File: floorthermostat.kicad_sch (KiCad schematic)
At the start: 29 parts, among them J1 Temp sensor socket 3 pin, J2 spi7segdisp, J3 Conn_01x06_Socket, J5 Programmin connector, Q1 BC549, SW1 Reset pushbutton, SW2 Enable pushbutton, U1 ESP32-WROOM-32, U2 GOLD 240V 3A SSR, U3 BD33FC0FP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

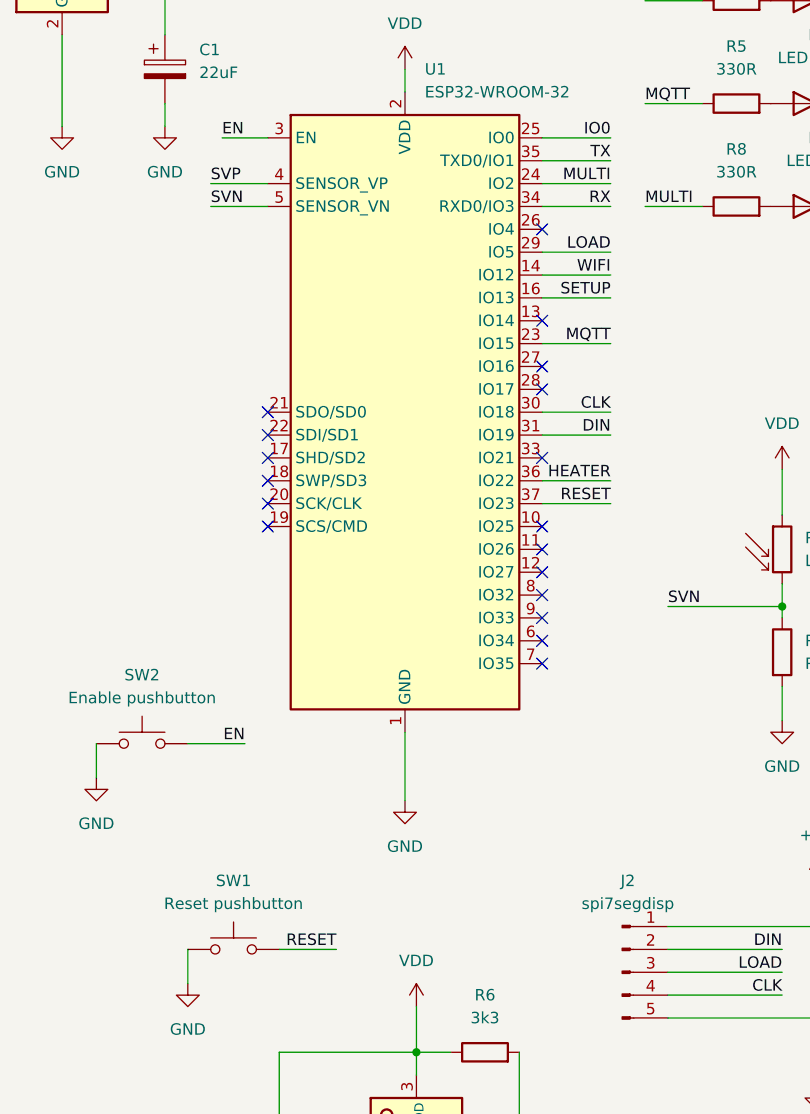
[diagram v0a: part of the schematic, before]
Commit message: Changed pcb to dual-sided.
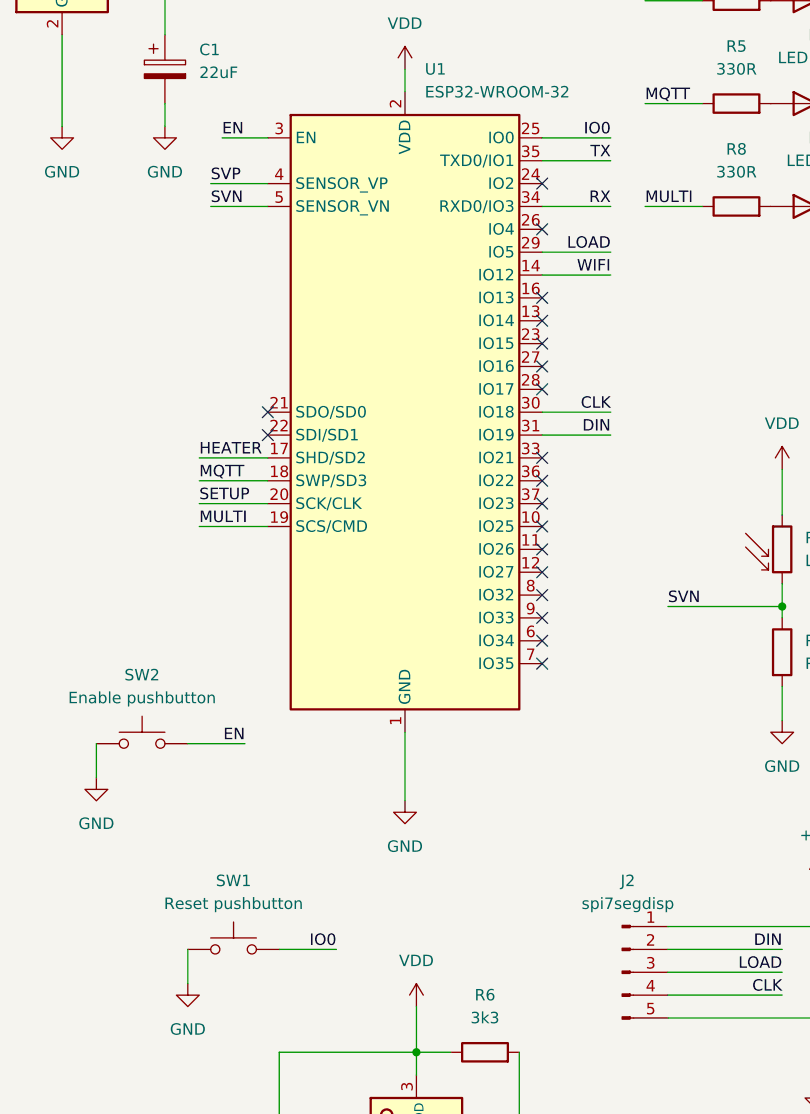
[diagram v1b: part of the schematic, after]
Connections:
- net HEATER: now also U1.17 (SHD/SD2); no longer U1.36 (IO22)
- net IO0: now also SW1.2
- net MQTT: now also U1.18 (SWP/SD3); no longer U1.23 (IO15)
- net MULTI: now also U1.19 (SCS/CMD); no longer U1.24 (IO2)
- net SETUP: now also U1.20 (SCK/CLK); no longer U1.16 (IO13)
- net RESET: no longer names the net of U1.37 (IO23)
- net RESET: no longer SW1.2
- no-connect marks 18 -> 19
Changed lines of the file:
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@@
+	)
+	(no_connect
+		(at 128.27 54.61)
 	)
 	(no_connect
@@
 	)
 	(no_connect
-		(at 97.79 87.63)
-	)
-	(no_connect
 		(at 128.27 69.85)
 	)
@@
 	)
 	(no_connect
+		(at 128.27 72.39)
+	)
+	(no_connect
 		(at 97.79 82.55)
 	)
@@
 	)
 	(no_connect
+		(at 128.27 90.17)
+	)
+	(no_connect
+		(at 128.27 67.31)
+	)
+	(no_connect
+		(at 128.27 105.41)
+	)
+	(no_connect
+		(at 128.27 74.93)
+	)
+	(no_connect
+		(at 128.27 85.09)
+	)
+	(no_connect
+		(at 128.27 59.69)
+	)
+	(no_connect
 		(at 128.27 77.47)
 	)
 	(no_connect
-		(at 97.79 90.17)
-	)
-	(no_connect
-		(at 128.27 105.41)
-	)
-	(no_connect
-		(at 128.27 74.93)
-	)
-	(no_connect
-		(at 128.27 85.09)
-	)
-	(no_connect
-		(at 128.27 59.69)
-	)
-	(no_connect
 		(at 128.27 92.71)
 	)
@@
 	)
 	(no_connect
-		(at 97.79 92.71)
-	)
-	(no_connect
 		(at 128.27 107.95)
 	)
@@
 	)
 	(no_connect
-		(at 97.79 85.09)
+		(at 128.27 87.63)
 	)
 	(wire
@@
 	(wire
 		(pts
-			(xy 128.27 90.17) (xy 135.89 90.17)
-		)
-		(stroke
-			(width 0)
-			(type default)
-		)
-	)
-	(wire
-		(pts
 			(xy 63.5 30.48) (xy 67.31 30.48)
 		)
@@
 	(wire
 		(pts
+			(xy 90.17 90.17) (xy 97.79 90.17)
+		)
+		(stroke
+			(width 0)
+			(type default)
+		)
+	)
+	(wire
+		(pts
 			(xy 125.73 175.26) (xy 125.73 161.29)
 		)
@@
 	(wire
 		(pts
-			(xy 128.27 87.63) (xy 135.89 87.63)
-		)
-		(stroke
-			(width 0)
-			(type default)
-		)
-	)
-	(wire
-		(pts
 			(xy 232.41 67.31) (xy 224.79 67.31)
 		)
@@
 	(wire
 		(pts
+			(xy 90.17 85.09) (xy 97.79 85.09)
+		)
+		(stroke
+			(width 0)
+			(type default)
+		)
+	)
+	(wire
+		(pts
 			(xy 92.71 177.8) (xy 114.3 177.8)
 		)
@@
 	(wire
 		(pts
-			(xy 128.27 54.61) (xy 135.89 54.61)
-		)
-		(stroke
-			(width 0)
-			(type default)
-		)
-	)
-	(wire
-		(pts
 			(xy 224.79 96.52) (xy 232.41 96.52)
 		)
@@
 	(wire
 		(pts
-			(xy 128.27 72.39) (xy 135.89 72.39)
-		)
-		(stroke
-			(width 0)
-			(type default)
-		)
-	)
-	(wire
-		(pts
-			(xy 128.27 67.31) (xy 135.89 67.31)
-		)
-		(stroke
-			(width 0)
-			(type default)
-		)
-	)
-	(wire
-		(pts
 			(xy 74.93 38.1) (xy 74.93 48.26)
 		)
@@
 	(wire
 		(pts
+			(xy 90.17 92.71) (xy 97.79 92.71)
+		)
+		(stroke
+			(width 0)
+			(type default)
+		)
+	)
+	(wire
+		(pts
 			(xy 207.01 46.99) (xy 207.01 50.8)
 		)
@@
 		(pts
 			(xy 229.87 60.96) (xy 232.41 60.96)
+		)
+		(stroke
+			(width 0)
+			(type default)
+		)
+	)
+	(wire
+		(pts
+			(xy 90.17 87.63) (xy 97.79 87.63)
 		)
 		(stroke
@@
 		)
 	)
-	(label "RESET"
-		(at 135.89 90.17 180)
-		(fields_autoplaced yes)
-		(effects
-			(font
-				(size 1.27 1.27)
-			)
-			(justify right bottom)
-		)
-	)
 	(label "LOAD"
 		(at 154.94 142.24 180)
@@
 	)
 	(label "SETUP"
-		(at 135.89 67.31 180)
-		(fields_autoplaced yes)
-		(effects
-			(font
-				(size 1.27 1.27)
-			)
-			(justify right bottom)
+		(at 90.17 90.17 0)
+		(fields_autoplaced yes)
+		(effects
+			(font
+				(size 1.27 1.27)
+			)
+			(justify left bottom)
+		)
+	)
+	(label "MQTT"
+		(at 90.17 87.63 0)
+		(fields_autoplaced yes)
+		(effects
+			(font
+				(size 1.27 1.27)
+			)
+			(justify left bottom)
+		)
+	)
+	(label "HEATER"
+		(at 90.17 85.09 0)
+		(fields_autoplaced yes)
+		(effects
+			(font
+				(size 1.27 1.27)
+			)
+			(justify left bottom)
 		)
 	)
@@
 		)
 	)
+	(label "MULTI"
+		(at 90.17 92.71 0)
+		(fields_autoplaced yes)
+		(effects
+			(font
+				(size 1.27 1.27)
+			)
+			(justify left bottom)
+		)
+	)
 	(label "WIFI"
 		(at 135.89 64.77 180)
@@
 		)
 	)
-	(label "MULTI"
-		(at 135.89 54.61 180)
-		(fields_autoplaced yes)
-		(effects
-			(font
-				(size 1.27 1.27)
-			)
-			(justify right bottom)
-		)
-	)
 	(label "IO0"
 		(at 213.36 41.91 180)
@@
 		)
 	)
-	(label "MQTT"
-		(at 135.89 72.39 180)
-		(fields_autoplaced yes)
-		(effects
-			(font
-				(size 1.27 1.27)
-			)
-			(justify right bottom)
-		)
-	)
 	(label "IO0"
 		(at 135.89 49.53 180)
@@
 		)
 	)
-	(label "HEATER"
-		(at 135.89 87.63 180)
-		(fields_autoplaced yes)
-		(effects
-			(font
-				(size 1.27 1.27)
-			)
-			(justify right bottom)
-		)
-	)
 	(label "ACN"
 		(at 217.17 119.38 0)
@@
 		)
 	)
-	(label "RESET"
+	(label "IO0"
 		(at 105.41 139.7 180)
 		(fields_autoplaced yes)
